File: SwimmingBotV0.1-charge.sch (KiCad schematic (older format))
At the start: 17 parts, among them P3 CHRG, P4 BATT, P5 DEBUG_JUMPER, Q1 Q_NMOS_DGS, Q2 Q_PMOS_DGS, Q3 Q_NMOS_DGS, U2 MCP73834

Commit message: hoh, working on power stuffs now
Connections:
- net 2S: no longer P4.4 (P4), P5.1
- new net 2S_RAW: P4.4 (P4), P5.1
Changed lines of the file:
@@
 Text Label 6150 4000 2    60   ~ 0
 1S
-Text Label 5800 3800 2    60   ~ 0
+Text Label 6500 3800 2    60   ~ 0
 2S
 $Comp
@@
 Wire Wire Line
 	6550 3800 6450 3800
+Text Label 5800 3800 0    60   ~ 0
+2S_RAW
 $EndSCHEMATC

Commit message: not final, moving towards board v0.2
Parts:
- removed P5: DEBUG_JUMPER, Socket_Strips:Socket_Strip_Straight_1x02, symbol JUMPER
- added R? (x2): 10k, Resistors_SMD:R_0402, symbol R
- R1: value 10k -> 5k
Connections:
- net 2S_RAW is gone; now on net 2S: P4.4 (P4)
- net 2S_EN: now also R?.2
- net 5V_CHG: now also R?.1
- net CHG_EN#: no longer U2.6 (PROG)
- net GND: now also R?.1; no longer R1.2
- net CHG_TE#: no longer names the net of U2.7 (TE#)
- net CHG_TE#: now also R?.2
- new net: R1.2, U2.6 (PROG)
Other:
- note added: "DIDN"T WORK\n\nMAGNETS ON OUTSIDE INSTEAD?"
- note added: "Replace with ic"
- note added: "can't get micro higher than 1s to turn this fet on duh"
- moved on the sheet: R1

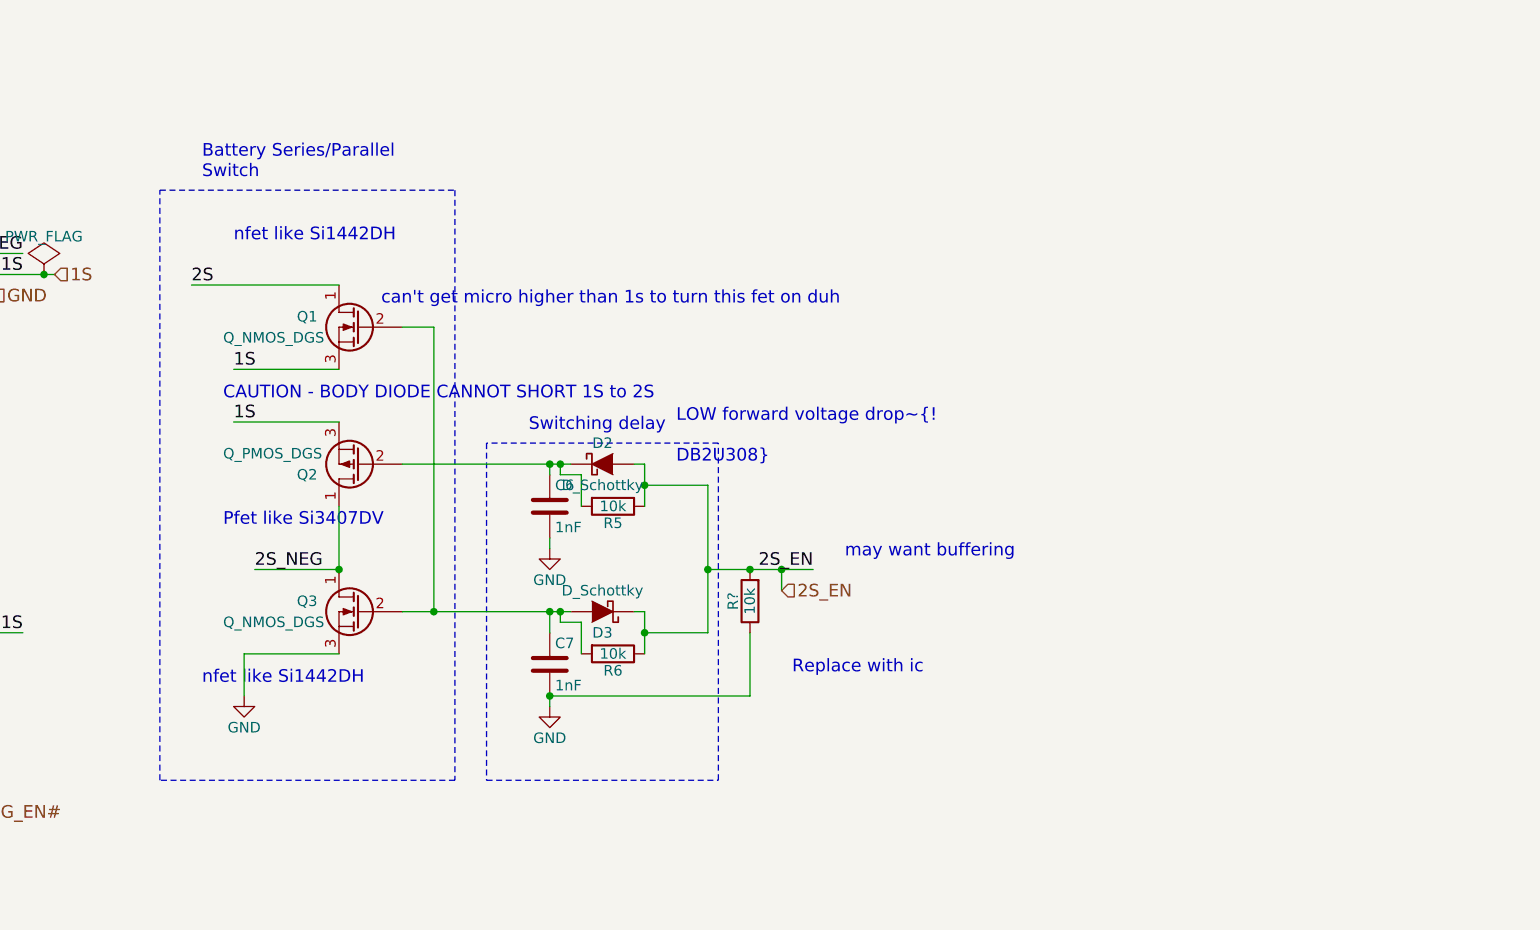
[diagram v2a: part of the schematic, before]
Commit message: swapped out battery serializing hardware from discrete to IC, and standard level fets
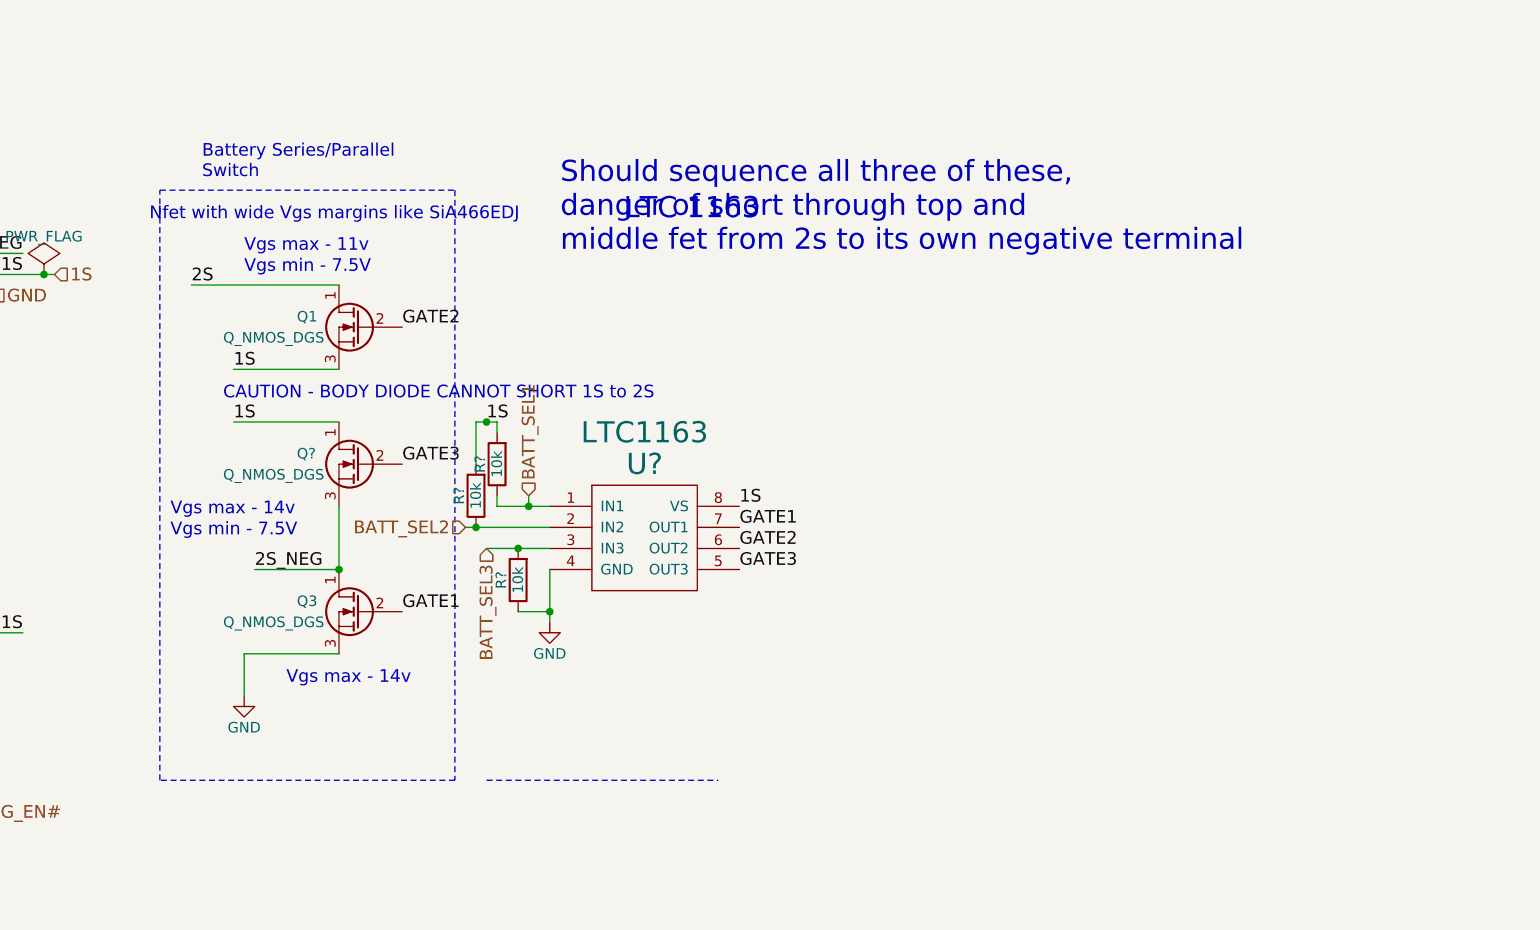
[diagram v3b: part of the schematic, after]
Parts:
- removed C6, C7: 1nF, Capacitors_SMD:C_0402, symbol C
- removed D2, D3: D_Schottky, Custom_Footprints:D_0402_SOD_923, symbol D_Schottky
- removed Q2: Q_PMOS_DGS, Custom_Footprints:TSOP-6_Si3407DV, symbol Q_PMOS_DGS
- removed R5, R6: 10k, Resistors_SMD:R_0402, symbol R
- added Q?: Q_NMOS_DGS, Custom_Footprints:SC-70-6-DGS, symbol Q_NMOS_DGS
- added R? (x2): 10k, Resistors_SMD:R_0402, symbol R
- added U?: LTC1163, symbol LTC1163
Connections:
- net 1S: now also Q?.1 (D), R?.2, R?.2, U?.8 (VS)
- net 2S_NEG: now also Q?.3 (S)
- net GND: now also U?.4 (GND)
- net GATE1: now reaches Q3.2 (G)
- net GATE1: now also U?.7 (OUT1); no longer Q1.2 (G)
- net 2S_EN renamed BATT_SEL3
- net BATT_SEL3: now also U?.3 (IN3)
- new net BATT_SEL1: R?.1, U?.1 (IN1)
- new net BATT_SEL2: R?.1, U?.2 (IN2)
- new net GATE2: Q1.2 (G), U?.6 (OUT2)
- new net GATE3: Q?.2 (G), U?.5 (OUT3)
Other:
- note added: "LTC 1163\n"
- note added: "Nfet with wide Vgs margins like SiA466EDJ"
- note added: "Should sequence all three of these, \ndanger of short through top and \nmiddle fet from 2s to its own negative terminal"
- note added: "Vgs max - 11v"
- note added: "Vgs max - 14v"
- note added: "Vgs min - 7.5V"
- note removed: "LOW forward voltage drop~!\n\nDB2U308"
- note removed: "Pfet like Si3407DV"
- note removed: "Replace with ic"
- note removed: "Switching delay"
- note removed: "can't get micro higher than 1s to turn this fet on duh"
- note removed: "may want buffering"
- note removed: "nfet like Si1442DH"
- moved on the sheet: R?

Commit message: potentially done with parts removal and reselection, on to pcb layout
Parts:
- gave numbers to parts that had none: 6
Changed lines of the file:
@@
 5V_CHG
 $Comp
-L GND #PWR04
+L GND #PWR4
 U 1 1 56CCCE56
 P 4000 4050
-F 0 "#PWR04" H 4000 3800 50  0001 C CNN
+F 0 "#PWR4" H 4000 3800 50  0001 C CNN
 F 1 "GND" H 4000 3900 50  0000 C CNN
 F 2 "" H 4000 4050 50  0000 C CNN
@@
 2S
 $Comp
-L GND #PWR05
+L GND #PWR5
 U 1 1 56CCD3F6
 P 5800 4200
-F 0 "#PWR05" H 5800 3950 50  0001 C CNN
+F 0 "#PWR5" H 5800 3950 50  0001 C CNN
 F 1 "GND" H 5800 4050 50  0000 C CNN
 F 2 "" H 5800 4200 50  0000 C CNN
@@
 5V_CHG
 $Comp
-L GND #PWR06
+L GND #PWR3
 U 1 1 56CCD61D
 P 3650 7300
-F 0 "#PWR06" H 3650 7050 50  0001 C CNN
+F 0 "#PWR3" H 3650 7050 50  0001 C CNN
 F 1 "GND" H 3650 7150 50  0000 C CNN
 F 2 "" H 3650 7300 50  0000 C CNN
@@
 Battery Series/Parallel\nSwitch
 $Comp
-L GND #PWR07
+L GND #PWR6
 U 1 1 56CCDFB0
 P 7200 6000
-F 0 "#PWR07" H 7200 5750 50  0001 C CNN
+F 0 "#PWR6" H 7200 5750 50  0001 C CNN
 F 1 "GND" H 7200 5850 50  0000 C CNN
 F 2 "" H 7200 6000 50  0000 C CNN
@@
 1S
 $Comp
-L GND #PWR08
+L GND #PWR7
 U 1 1 56CDD8C1
 P 8650 5650
-F 0 "#PWR08" H 8650 5400 50  0001 C CNN
+F 0 "#PWR7" H 8650 5400 50  0001 C CNN
 F 1 "GND" H 8650 5500 50  0000 C CNN
 F 2 "" H 8650 5650 50  0000 C CNN
@@
 $EndComp
 $Comp
-L PWR_FLAG #FLG010
+L PWR_FLAG #FLG2
 U 1 1 57591160
 P 4050 3900
-F 0 "#FLG010" H 4050 3995 50  0001 C CNN
+F 0 "#FLG2" H 4050 3995 50  0001 C CNN
 F 1 "PWR_FLAG" H 4050 4080 50  0000 C CNN
 F 2 "" H 4050 3900 50  0000 C CNN
@@
 $EndComp
 $Comp
-L PWR_FLAG #FLG011
+L PWR_FLAG #FLG3
 U 1 1 57594C3B
 P 5700 3800
-F 0 "#FLG011" H 5700 3895 50  0001 C CNN
+F 0 "#FLG3" H 5700 3895 50  0001 C CNN
 F 1 "PWR_FLAG" H 5700 3980 50  0000 C CNN
 F 2 "" H 5700 3800 50  0000 C CNN
@@
 $EndComp
 $Comp
-L PWR_FLAG #FLG012
+L PWR_FLAG #FLG4
 U 1 1 57594C80
 P 6250 4000
-F 0 "#FLG012" H 6250 4095 50  0001 C CNN
+F 0 "#FLG4" H 6250 4095 50  0001 C CNN
 F 1 "PWR_FLAG" H 6250 4180 50  0000 C CNN
 F 2 "" H 6250 4000 50  0000 C CNN
@@
 $EndComp
 $Comp
-L R R?
+L R R23
 U 1 1 57478D73
 P 8500 5450
-F 0 "R?" V 8580 5450 50  0000 C CNN
+F 0 "R23" V 8580 5450 50  0000 C CNN
 F 1 "10k" V 8500 5450 50  0000 C CNN
 F 2 "Resistors_SMD:R_0402" V 8430 5450 50  0001 C CNN
@@
 $EndComp
 $Comp
-L R R?
+L R R14
 U 1 1 5790B62F
 P 4750 6800
-F 0 "R?" V 4830 6800 50  0000 C CNN
+F 0 "R14" V 4830 6800 50  0000 C CNN
 F 1 "10k" V 4750 6800 50  0000 C CNN
 F 2 "Resistors_SMD:R_0402" V 4680 6800 50  0001 C CNN
@@
 Should sequence all three of these, \ndanger of short through top and \nmiddle fet from 2s to its own negative terminal
 $Comp
-L R R?
+L R R21
 U 1 1 5798EA84
 P 8300 5050
-F 0 "R?" V 8380 5050 50  0000 C CNN
+F 0 "R21" V 8380 5050 50  0000 C CNN
 F 1 "10k" V 8300 5050 50  0000 C CNN
 F 2 "Resistors_SMD:R_0402" V 8230 5050 50  0001 C CNN
@@
 $EndComp
 $Comp
-L R R?
+L R R22
 U 1 1 5798EADC
 P 8400 4900
-F 0 "R?" V 8480 4900 50  0000 C CNN
+F 0 "R22" V 8480 4900 50  0000 C CNN
 F 1 "10k" V 8400 4900 50  0000 C CNN
 F 2 "Resistors_SMD:R_0402" V 8330 4900 50  0001 C CNN
@@
 1S
 $Comp
-L LTC1163 U?
+L LTC1163 U13
 U 1 1 5798EFC2
 P 9100 5300
-F 0 "U?" H 9100 5700 100 0000 C CNN
+F 0 "U13" H 9100 5700 100 0000 C CNN
 F 1 "LTC1163" H 9100 5850 100 0000 C CNN
 F 2 "" H 9100 5300 100 0000 C CNN
@@
 Connection ~ 8350 4700
 $Comp
-L Q_NMOS_DGS Q?
+L Q_NMOS_DGS Q2
 U 1 1 5798F6B7
 P 7750 4900
-F 0 "Q?" H 8050 4950 50  0000 R CNN
+F 0 "Q2" H 8050 4950 50  0000 R CNN
 F 1 "Q_NMOS_DGS" H 8400 4850 50  0000 R CNN
 F 2 "Custom_Footprints:SC-70-6-DGS" H 7950 5000 50  0001 C CNN

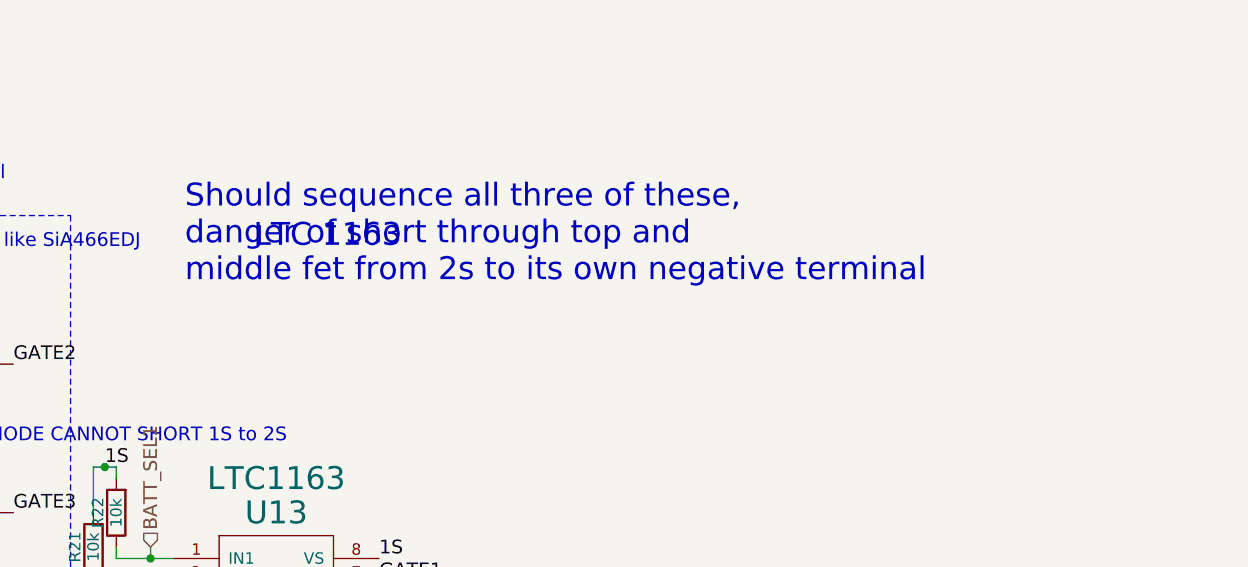
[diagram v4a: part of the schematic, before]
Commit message: pcb started in earnest, footprint changes in schematics, about to rename v0.2 boardfile to v0.1, kicad needs the same filename to have backrefs for net highlighting
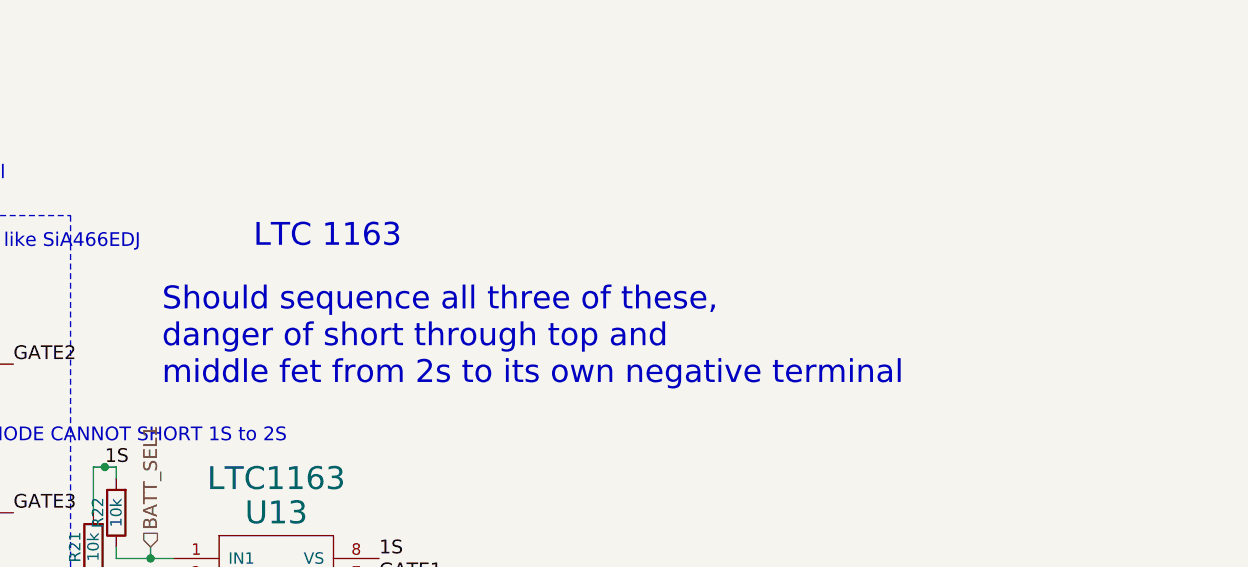
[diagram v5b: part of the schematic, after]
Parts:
- Q1, Q2, Q3: footprint Custom_Footprints:SC-70-6-DGS -> Custom_Footprints:SC-70-ENHANCED-DGS
- U13: footprint (none) -> SMD_Packages:SOIC-8-N
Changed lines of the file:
@@
 5V_CHG
 $Comp
-L GND #PWR4
+L GND #PWR04
 U 1 1 56CCCE56
 P 4000 4050
-F 0 "#PWR4" H 4000 3800 50  0001 C CNN
+F 0 "#PWR04" H 4000 3800 50  0001 C CNN
 F 1 "GND" H 4000 3900 50  0000 C CNN
 F 2 "" H 4000 4050 50  0000 C CNN
@@
 2S
 $Comp
-L GND #PWR5
+L GND #PWR05
 U 1 1 56CCD3F6
 P 5800 4200
-F 0 "#PWR5" H 5800 3950 50  0001 C CNN
+F 0 "#PWR05" H 5800 3950 50  0001 C CNN
 F 1 "GND" H 5800 4050 50  0000 C CNN
 F 2 "" H 5800 4200 50  0000 C CNN
@@
 5V_CHG
 $Comp
-L GND #PWR3
+L GND #PWR06
 U 1 1 56CCD61D
 P 3650 7300
-F 0 "#PWR3" H 3650 7050 50  0001 C CNN
+F 0 "#PWR06" H 3650 7050 50  0001 C CNN
 F 1 "GND" H 3650 7150 50  0000 C CNN
 F 2 "" H 3650 7300 50  0000 C CNN
@@
 Battery Series/Parallel\nSwitch
 $Comp
-L GND #PWR6
+L GND #PWR07
 U 1 1 56CCDFB0
 P 7200 6000
-F 0 "#PWR6" H 7200 5750 50  0001 C CNN
+F 0 "#PWR07" H 7200 5750 50  0001 C CNN
 F 1 "GND" H 7200 5850 50  0000 C CNN
 F 2 "" H 7200 6000 50  0000 C CNN
@@
 1S
 $Comp
-L GND #PWR7
+L GND #PWR08
 U 1 1 56CDD8C1
 P 8650 5650
-F 0 "#PWR7" H 8650 5400 50  0001 C CNN
+F 0 "#PWR08" H 8650 5400 50  0001 C CNN
 F 1 "GND" H 8650 5500 50  0000 C CNN
 F 2 "" H 8650 5650 50  0000 C CNN
@@
 F 0 "Q1" H 8050 4300 50  0000 R CNN
 F 1 "Q_NMOS_DGS" H 8400 4200 50  0000 R CNN
-F 2 "Custom_Footprints:SC-70-6-DGS" H 7950 4350 50  0001 C CNN
+F 2 "Custom_Footprints:SC-70-ENHANCED-DGS" H 7950 4350 50  0001 C CNN
 F 3 "" H 7750 4250 50  0000 C CNN
 	1    7750 4250
@@
 F 0 "Q3" H 8050 5650 50  0000 R CNN
 F 1 "Q_NMOS_DGS" H 8400 5550 50  0000 R CNN
-F 2 "Custom_Footprints:SC-70-6-DGS" H 7950 5700 50  0001 C CNN
+F 2 "Custom_Footprints:SC-70-ENHANCED-DGS" H 7950 5700 50  0001 C CNN
 F 3 "" H 7750 5600 50  0000 C CNN
 	1    7750 5600
@@
 $EndComp
 $Comp
-L PWR_FLAG #FLG2
+L PWR_FLAG #FLG09
 U 1 1 57591160
 P 4050 3900
-F 0 "#FLG2" H 4050 3995 50  0001 C CNN
+F 0 "#FLG09" H 4050 3995 50  0001 C CNN
 F 1 "PWR_FLAG" H 4050 4080 50  0000 C CNN
 F 2 "" H 4050 3900 50  0000 C CNN
@@
 $EndComp
 $Comp
-L PWR_FLAG #FLG3
+L PWR_FLAG #FLG010
 U 1 1 57594C3B
 P 5700 3800
-F 0 "#FLG3" H 5700 3895 50  0001 C CNN
+F 0 "#FLG010" H 5700 3895 50  0001 C CNN
 F 1 "PWR_FLAG" H 5700 3980 50  0000 C CNN
 F 2 "" H 5700 3800 50  0000 C CNN
@@
 $EndComp
 $Comp
-L PWR_FLAG #FLG4
+L PWR_FLAG #FLG011
 U 1 1 57594C80
 P 6250 4000
-F 0 "#FLG4" H 6250 4095 50  0001 C CNN
+F 0 "#FLG011" H 6250 4095 50  0001 C CNN
 F 1 "PWR_FLAG" H 6250 4180 50  0000 C CNN
 F 2 "" H 6250 4000 50  0000 C CNN
@@
 Text Notes 9000 3750 0    100  ~ 0
 LTC 1163\n
-Text Notes 8700 3900 0    100  ~ 0
+Text Notes 8600 4350 0    100  ~ 0
 Should sequence all three of these, \ndanger of short through top and \nmiddle fet from 2s to its own negative terminal
 $Comp
@@
 F 0 "U13" H 9100 5700 100 0000 C CNN
 F 1 "LTC1163" H 9100 5850 100 0000 C CNN
-F 2 "" H 9100 5300 100 0000 C CNN
+F 2 "SMD_Packages:SOIC-8-N" H 9100 5300 100 0001 C CNN
 F 3 "" H 9100 5300 100 0000 C CNN
 	1    9100 5300
@@
 F 0 "Q2" H 8050 4950 50  0000 R CNN
 F 1 "Q_NMOS_DGS" H 8400 4850 50  0000 R CNN
-F 2 "Custom_Footprints:SC-70-6-DGS" H 7950 5000 50  0001 C CNN
+F 2 "Custom_Footprints:SC-70-ENHANCED-DGS" H 7950 5000 50  0001 C CNN
 F 3 "" H 7750 4900 50  0000 C CNN
 	1    7750 4900

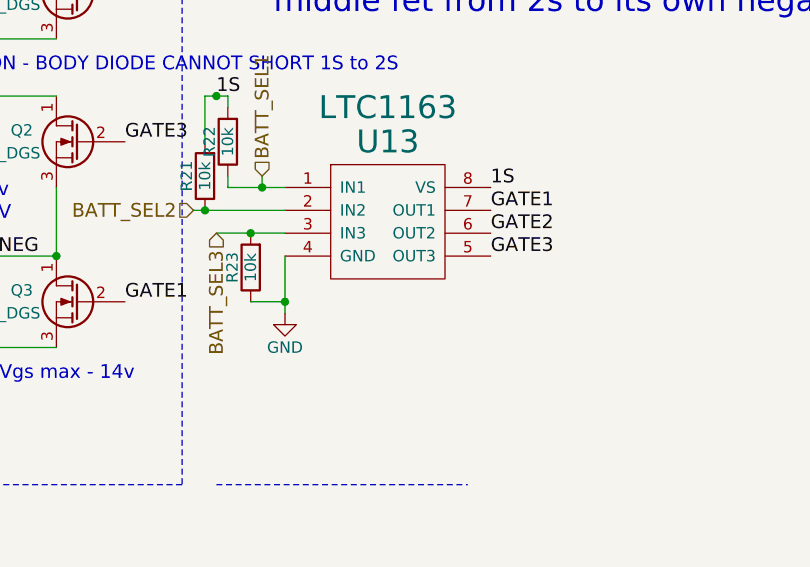
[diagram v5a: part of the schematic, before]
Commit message: some pin swaps for routing, done with power section
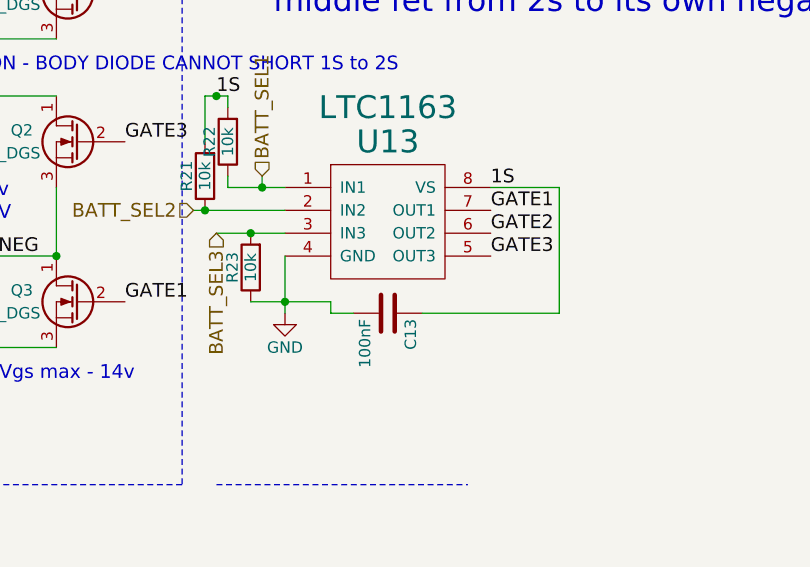
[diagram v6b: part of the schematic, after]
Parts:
- added C13: 100nF, Capacitors_SMD:C_0402, symbol C
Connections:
- net 1S: now also C13.1
- net GND: now also C13.2
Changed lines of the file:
@@
 	8650 5400 8650 5650
 Wire Wire Line
-	8500 5600 8650 5600
+	8500 5600 8850 5600
 Connection ~ 8650 5600
 Wire Wire Line
@@
 Text Notes 6750 3750 0    60   ~ 0
 Nfet with wide Vgs margins like SiA466EDJ
+$Comp
+L C C13
+U 1 1 57A2F2D2
+P 9100 5650
+F 0 "C13" H 9125 5750 50  0000 L CNN
+F 1 "100nF" H 9125 5550 50  0000 L CNN
+F 2 "Capacitors_SMD:C_0402" H 9138 5500 50  0001 C CNN
+F 3 "" H 9100 5650 50  0000 C CNN
+	1    9100 5650
+	0    1    1    0
+$EndComp
+Wire Wire Line
+	9550 5100 9850 5100
+Wire Wire Line
+	9850 5100 9850 5650
+Wire Wire Line
+	9850 5650 9250 5650
+Wire Wire Line
+	8950 5650 8850 5650
+Wire Wire Line
+	8850 5650 8850 5600
 $EndSCHEMATC
